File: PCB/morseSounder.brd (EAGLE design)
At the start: 56.6 x 82.7 mm, 67 parts, among them IC1 LM386M-1, IC3 MAT-02H, IC4 AVR-MEGA8-PPTH, IC5 LM321MF, IC6 MEGA16-A, J1 AVR_SPI_PRG_6PTH, J2 POWERPOLE_POWER25A_HORIZONTAL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, J3 POWER_JACKPTH, Q1 2N3904

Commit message: Replaced most through hole components with SMD equivilents
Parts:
- removed IC3: MAT-02H, linear:TO78
- removed IC4: AVR-MEGA8-PPTH, SparkFun:DIL28-3
- removed IC6: MEGA16-A, atmel:TQFP44
- added Q2, Q3: MMBT3904, transistor:SOT23-BEC
- added R16: 10K, SparkFun:0805
- added SJ1: SOLDERJUMPERNO, SparkFun:SJ_2S-NO
- added U1: ATMEGA168, SparkFun:TQFP32-08
- Q1: value 2N3904 -> MMBT3904; device transistor-npn:TO92 -> transistor:SOT23-BEC
- T1: value (none) -> MMBTA42; device transistor:TO92-EBC -> SparkFun:SOT23
- moved C17 315.3 mm to (53.3, 48.3)
- moved R31 309.7 mm to (53.3, 44.5), turned to 90 degrees
- moved C18 304.8 mm to (53.3, 40.6), turned to 90 degrees
- moved C20 298.0 mm to (7.62, 73.7)
- moved U$5 298.0 mm to (10.2, 73.7)
- moved C19 296.1 mm to (12.7, 73.7)
- moved R5 256.4 mm to (47.0, 27.9)
- moved R6 252.3 mm to (44.5, 27.9), turned to 90 degrees
- moved IC5 250.3 mm to (45.7, 22.9), turned to 270 degrees
- moved C5 245.8 mm to (45.7, 19.1), turned to 0 degrees
- moved R4 244.1 mm to (47.0, 16.5), turned to 180 degrees
- moved JP2 235.4 mm to (-14.0, 49.5), turned to 270 degrees
- moved R7 229.9 mm to (49.5, 39.4), turned to 270 degrees
- moved R13 219.3 mm to (43.2, 34.3), turned to 90 degrees
- moved R12 217.2 mm to (40.6, 34.3), turned to 90 degrees
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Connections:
- removed net AVCC: IC6.27
- removed net GND1: IC6.18
- removed net GND2: IC6.39
- removed net VCC: IC6.5
- removed net VCC1: IC6.17
- removed net VCC2: IC6.38
- new net N$14: SJ1.2, U$2.P$5
- net ADC_RATE: now also U1.24; no longer IC4.24
- net ADC_WEIGHT: now also U1.23; no longer IC4.23
- net AVR_DASH: now also U1.26; no longer IC4.26
- net AVR_DOT: now also U1.25; no longer IC4.25
- net AVR_KEY_MODE: now also R16.2, U1.28; no longer IC4.28
- net AVR_KEY_OUT: now also U1.27; no longer IC4.27
- net AVR_MISO: now also U1.16; no longer IC4.18
- net AVR_MOSI: now also U1.15; no longer IC4.17
- net AVR_RESET: now also U1.29; no longer IC4.1
- net AVR_RX: now also U1.30; no longer IC4.2
- net AVR_SCK: now also U1.17; no longer IC4.19
- net AVR_TX: now also U1.31; no longer IC4.3
- net AVR_VCC: now also R16.1, U1.18, U1.20, U1.4, U1.6; no longer IC4.20, IC4.21, IC4.7
- net GND: now also T1.2, U1.21, U1.3, U1.5; no longer IC4.22, IC4.8, IC6.28, IC6.6, T1.E
- net N$11: now also Q3.B; no longer IC3.5
- net N$13: now also Q1.E; no longer Q1.3
- net N$2: now also SJ1.1; no longer U$2.P$5
- net N$23: now also T1.3; no longer T1.C
- net N$24: now also T1.1; no longer T1.B
- net N$6: now also Q2.C; no longer IC3.1
- net N$7: now also Q3.C; no longer IC3.6
- net N$8: now also Q1.C, Q2.E, Q3.E; no longer IC3.3, IC3.4, Q1.1
- net N$9: now also Q1.B; no longer Q1.2
- net TONE_OUT: now also Q2.B; no longer IC3.2
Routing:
- net AVR_VCC: track 0.00 -> 66.8 mm, vias 0 -> 2
- net VIN: track 0.00 -> 53.3 mm
- net +12V: track 0.00 -> 49.9 mm
- net N$6: track 0.00 -> 32.5 mm, vias 0 -> 2
- net AUDIO_OUT: track 0.00 -> 30.4 mm, vias 0 -> 1
- net ADC_RATE: track 0.00 -> 28.6 mm
- net N$12: track 0.00 -> 26.7 mm, vias 0 -> 2
- net AVR_MOSI: track 0.00 -> 24.8 mm, vias 0 -> 2
- net TONE_OUT: track 0.00 -> 23.1 mm, vias 0 -> 2
- net AVR_SCK: track 0.00 -> 22.6 mm, vias 0 -> 1
- net N$7: track 0.00 -> 22.0 mm, vias 0 -> 2
- net ADC_WEIGHT: track 0.00 -> 21.7 mm
- net N$5: track 0.00 -> 20.7 mm
- net N$8: track 0.00 -> 18.9 mm, vias 0 -> 2
- net N$4: track 0.00 -> 13.3 mm
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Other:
- board text added: "Audio Amplifier"
- board text added: "DC IN 12V"
- board text added: "Oscilator"
- board text added: "PWR LED"
- board text added: "Voltage controled Amp"

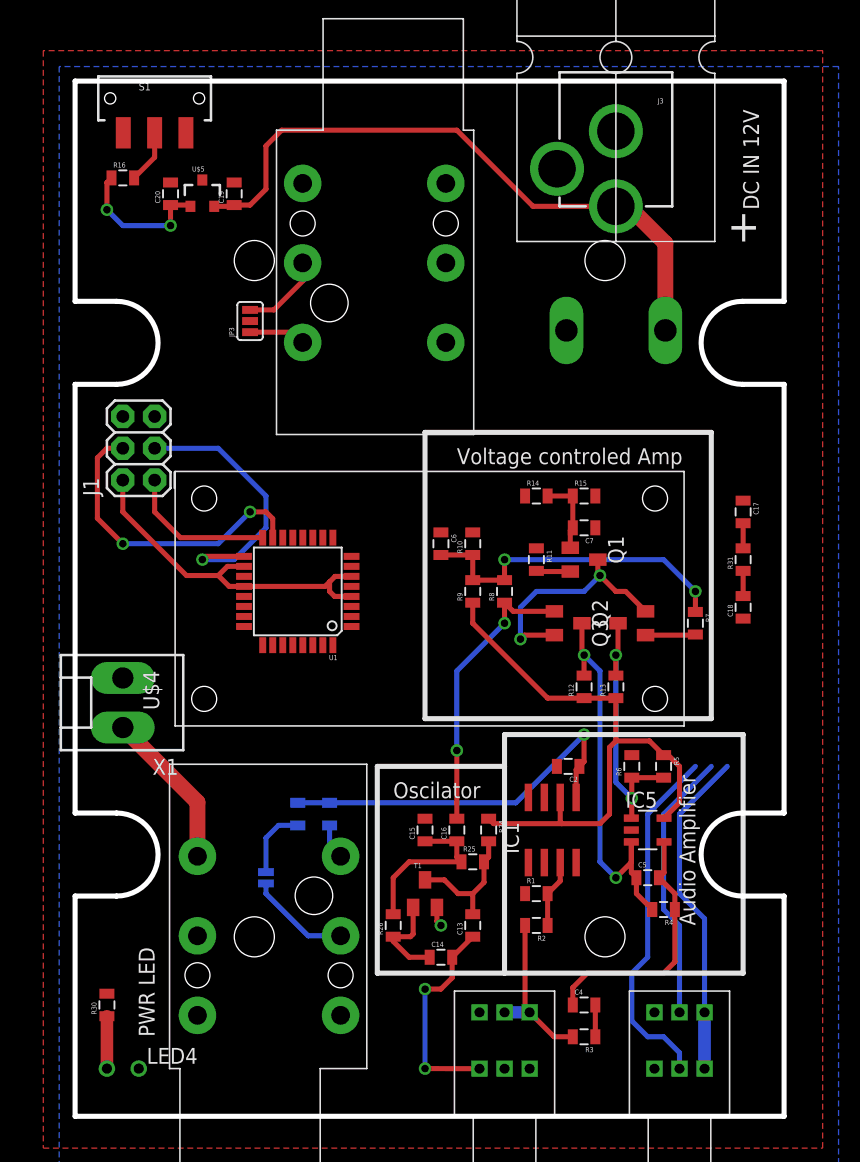
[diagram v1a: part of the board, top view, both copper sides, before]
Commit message: Tidied up silk screen on PCB
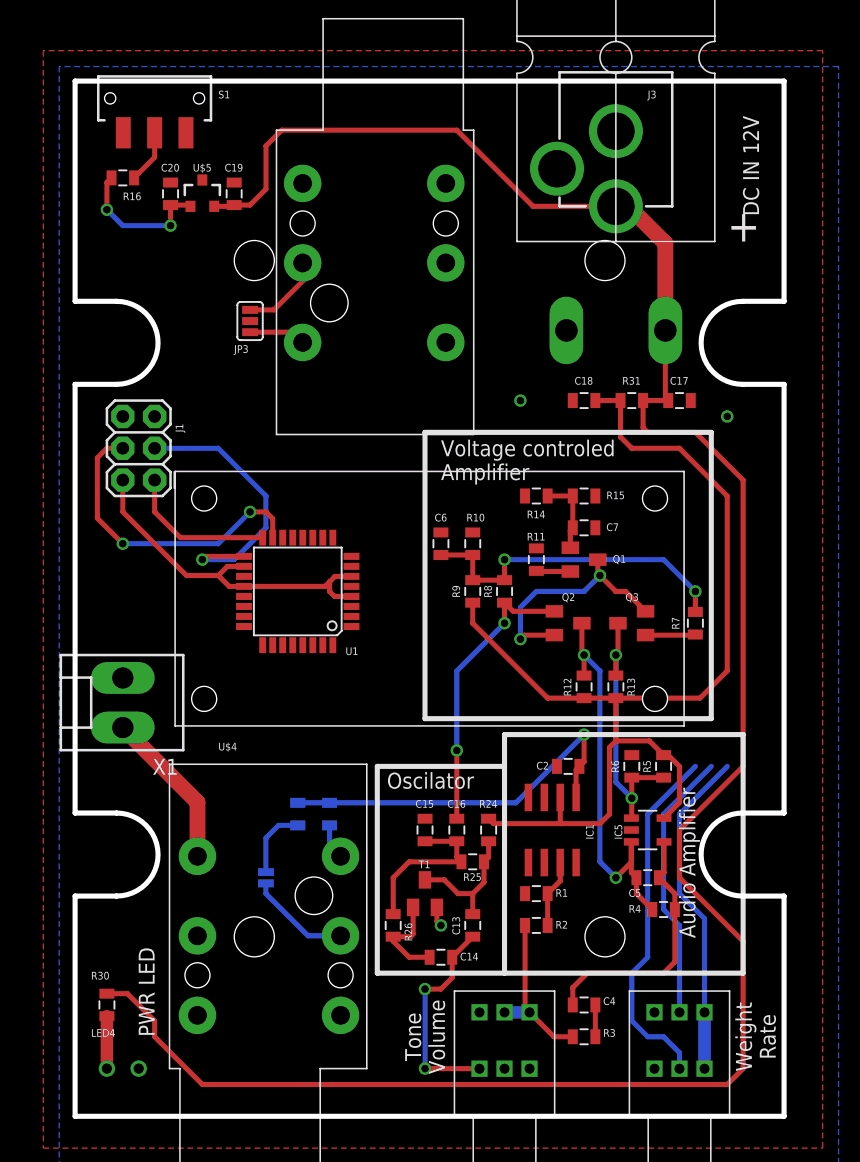
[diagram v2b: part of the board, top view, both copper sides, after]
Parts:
- moved C18 20.8 mm to (40.6, 57.1), turned to 0 degrees
- moved R31 15.5 mm to (44.5, 57.1), turned to 0 degrees
- moved C17 10.2 mm to (48.3, 57.1), turned to 180 degrees
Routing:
- net VIN: track 53.3 -> 177.1 mm
- net +12V: track 49.9 -> 87.0 mm
- net GND: vias 1 -> 3
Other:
- board text added: "Tone Volume"
- board text added: "Voltage controled Amplifier"
- board text added: "Weight Rate"
- board text removed: "Voltage controled Amp"

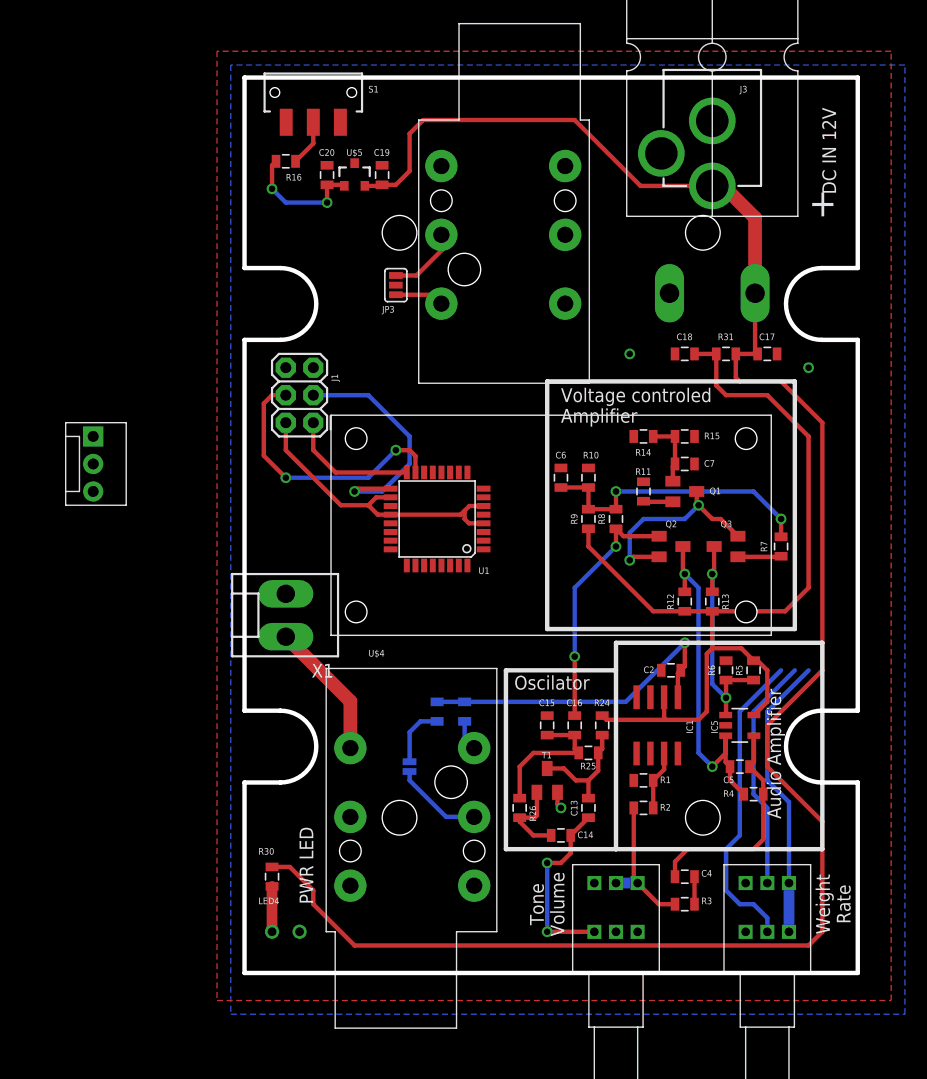
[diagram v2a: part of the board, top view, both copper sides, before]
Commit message: Added test points and cleaned up some silkscreen issues
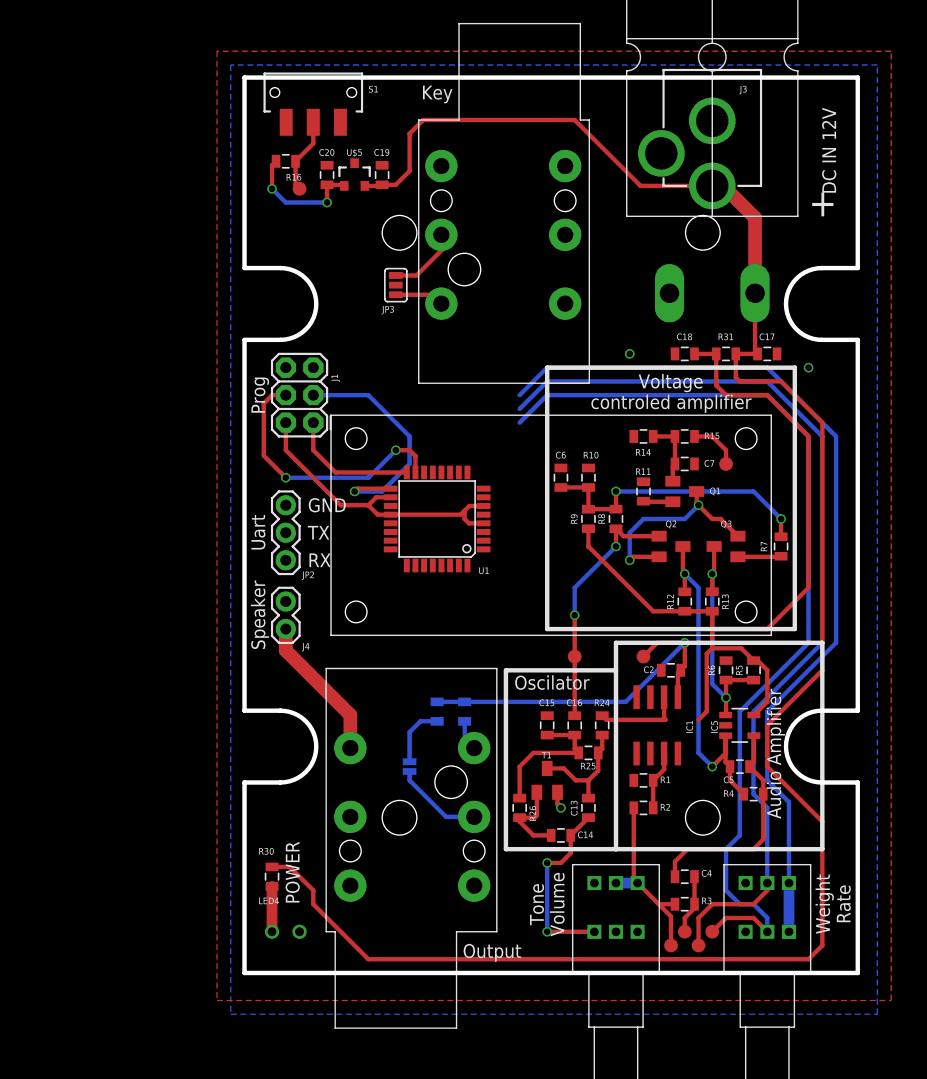
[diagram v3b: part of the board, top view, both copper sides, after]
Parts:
- removed X1: (no value), con-molex:KK-156-2
- added J4: (no value), SparkFun-Connectors:1X02
- added TP1, TP2, TP3, TP4, TP5, TP6, TP7, TP8: TEST-POINT3X5, SparkFun-Connectors:PAD.03X.05
- JP2: device SparkFun:MOLEX-1X3 -> SparkFun-Connectors:1X03
- moved JP2 21.1 mm to (3.81, 38.1), turned to 90 degrees
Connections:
- removed net N$4: R2.2, R3.2, U$3.R2, U$3.R3
- new net N$15: R2.2, R3.2, TP8.P$1, U$3.R2, U$3.R3
- net ADC_RATE: now also TP1.P$1
- net ADC_WEIGHT: now also TP2.P$1
- net AUDIO_OUT: now also TP4.P$1
- net AUDIO_PRE_AMP: now also TP5.P$1
- net AVR_KEY_MODE: now also TP3.P$1
- net GND: now also J4.2; no longer X1.2
- net KEY_IN: now also TP7.P$1
- net N$28: now also J4.1; no longer X1.1
- net TONE_OUT: now also TP6.P$1
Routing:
- net ADC_WEIGHT: track 21.7 -> 86.1 mm
- net ADC_RATE: track 28.6 -> 86.7 mm
- net AVR_VCC: track 66.8 -> 122.3 mm
- net N$15: track 0.00 -> 17.6 mm
- net N$4: track 13.3 -> 0.00 mm
- net KEY_IN: track 0.00 -> 4.71 mm
- net AUDIO_OUT: track 30.4 -> 34.7 mm
- net AUDIO_PRE_AMP: track 2.54 -> 5.45 mm
- net AVR_KEY_MODE: track 4.28 -> 6.97 mm
- net +12V: track 87.0 -> 84.6 mm
- net VIN: track 177.1 -> 178.9 mm
- net N$28: track 12.7 -> 13.5 mm
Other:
- board text added: "GND"
- board text added: "Key"
- board text added: "Output"
- board text added: "POWER"
- board text added: "Prog"
- board text added: "RX"
- board text added: "Speaker"
- board text added: "TX"
- board text added: "Uart"
- board text added: "Voltage controled amplifier"
- board text removed: "PWR LED"
- board text removed: "Voltage controled Amplifier"

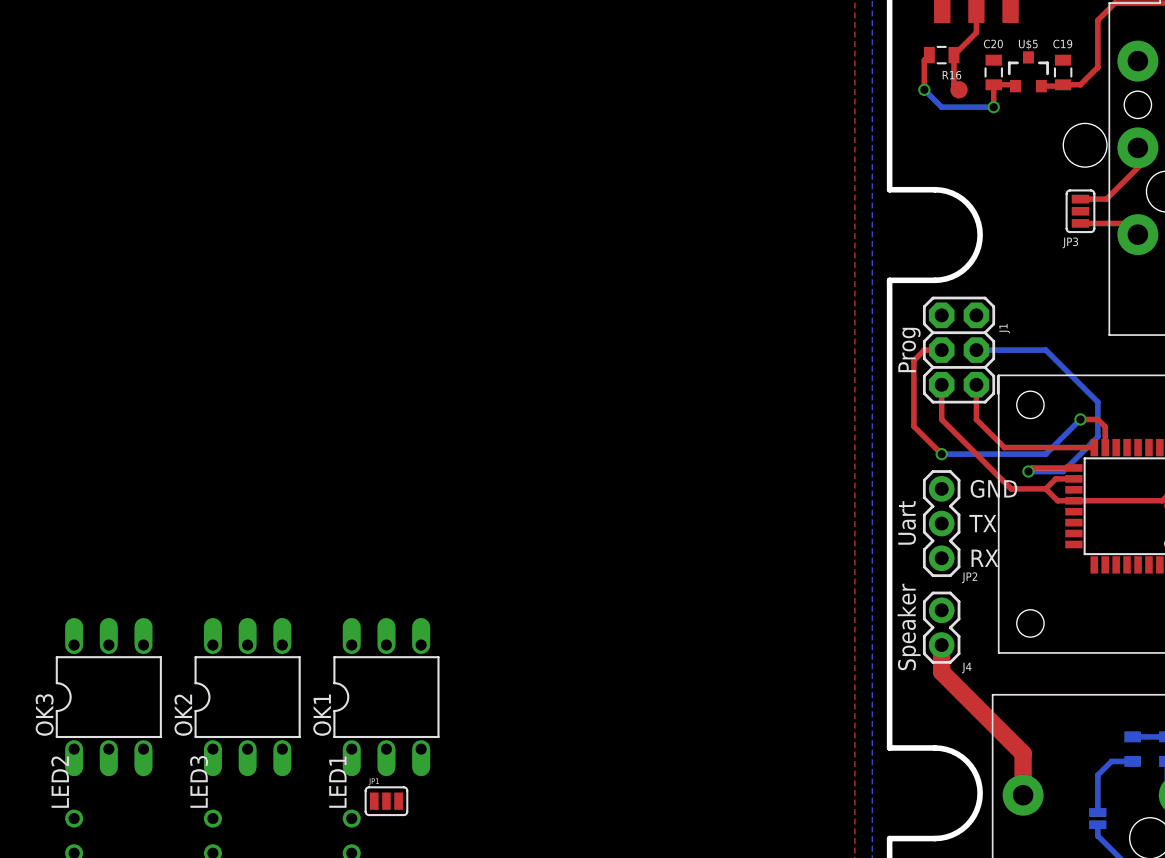
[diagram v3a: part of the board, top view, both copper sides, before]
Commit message: * Removed the pair of unused opto-isolators. * Commenced tidying up the schematic. & Removal of 3rd opto-isolator may prove tricky...
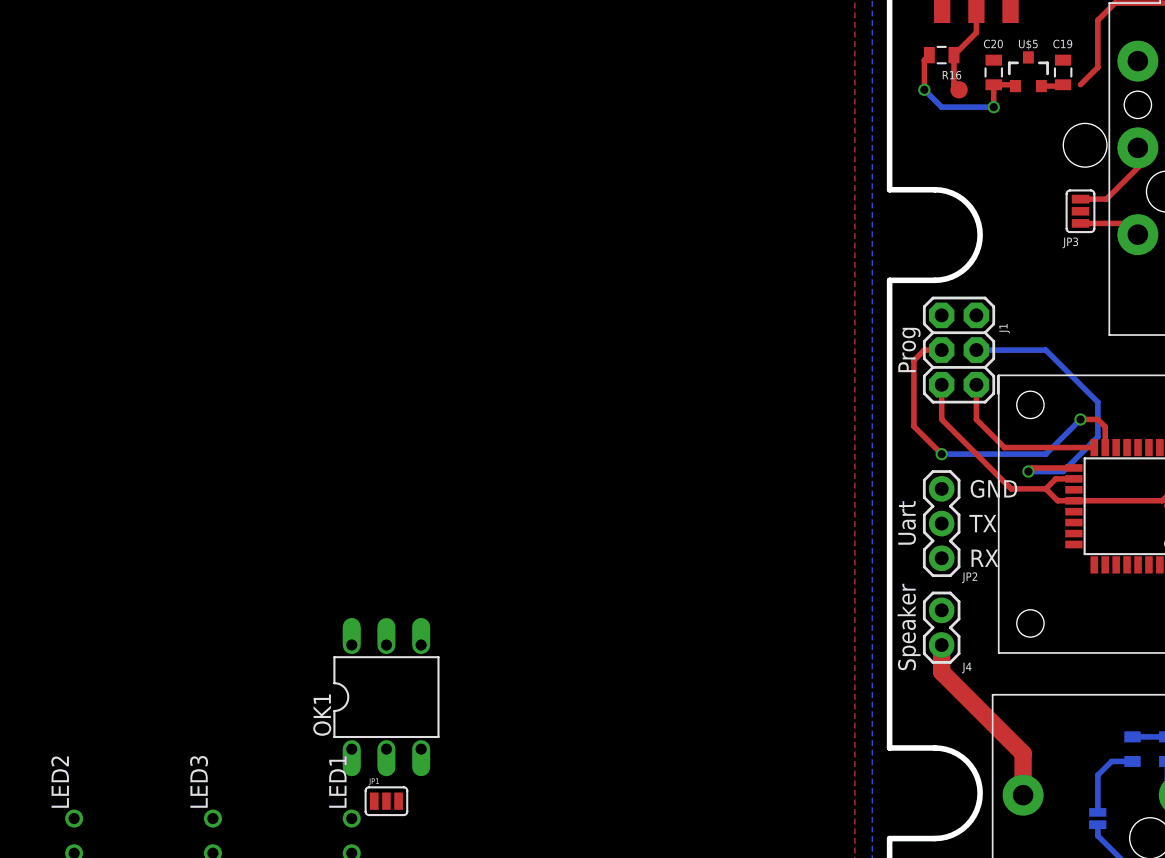
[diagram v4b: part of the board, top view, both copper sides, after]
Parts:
- removed OK2, OK3: 4N35, optocoupler:DIL06
- R28, R29: value 750 -> 330
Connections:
- removed net AVR_DASH: U1.26
- removed net AVR_DOT: U1.25
- removed net AVR_KEY_DASH: OK3.5
- removed net AVR_KEY_DOT: OK2.5
- removed net N$34: LED2.K, OK3.1
- removed net N$35: LED3.K, OK2.1
- net +12V: now also C19.1, U$5.2
- net GND: no longer OK2.4, OK3.4
- net KEY_DASH: now also LED3.K, U1.26; no longer OK3.2
- net KEY_DOT: now also LED2.K, U1.25; no longer OK2.2
- net VIN: no longer C19.1, U$5.2
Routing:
- net VIN: track 178.9 -> 176.0 mm
- net +12V: track 84.6 -> 86.3 mm
